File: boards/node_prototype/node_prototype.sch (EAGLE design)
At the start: 28 parts, among them T1 2N2222, X1 BU-SMA-H

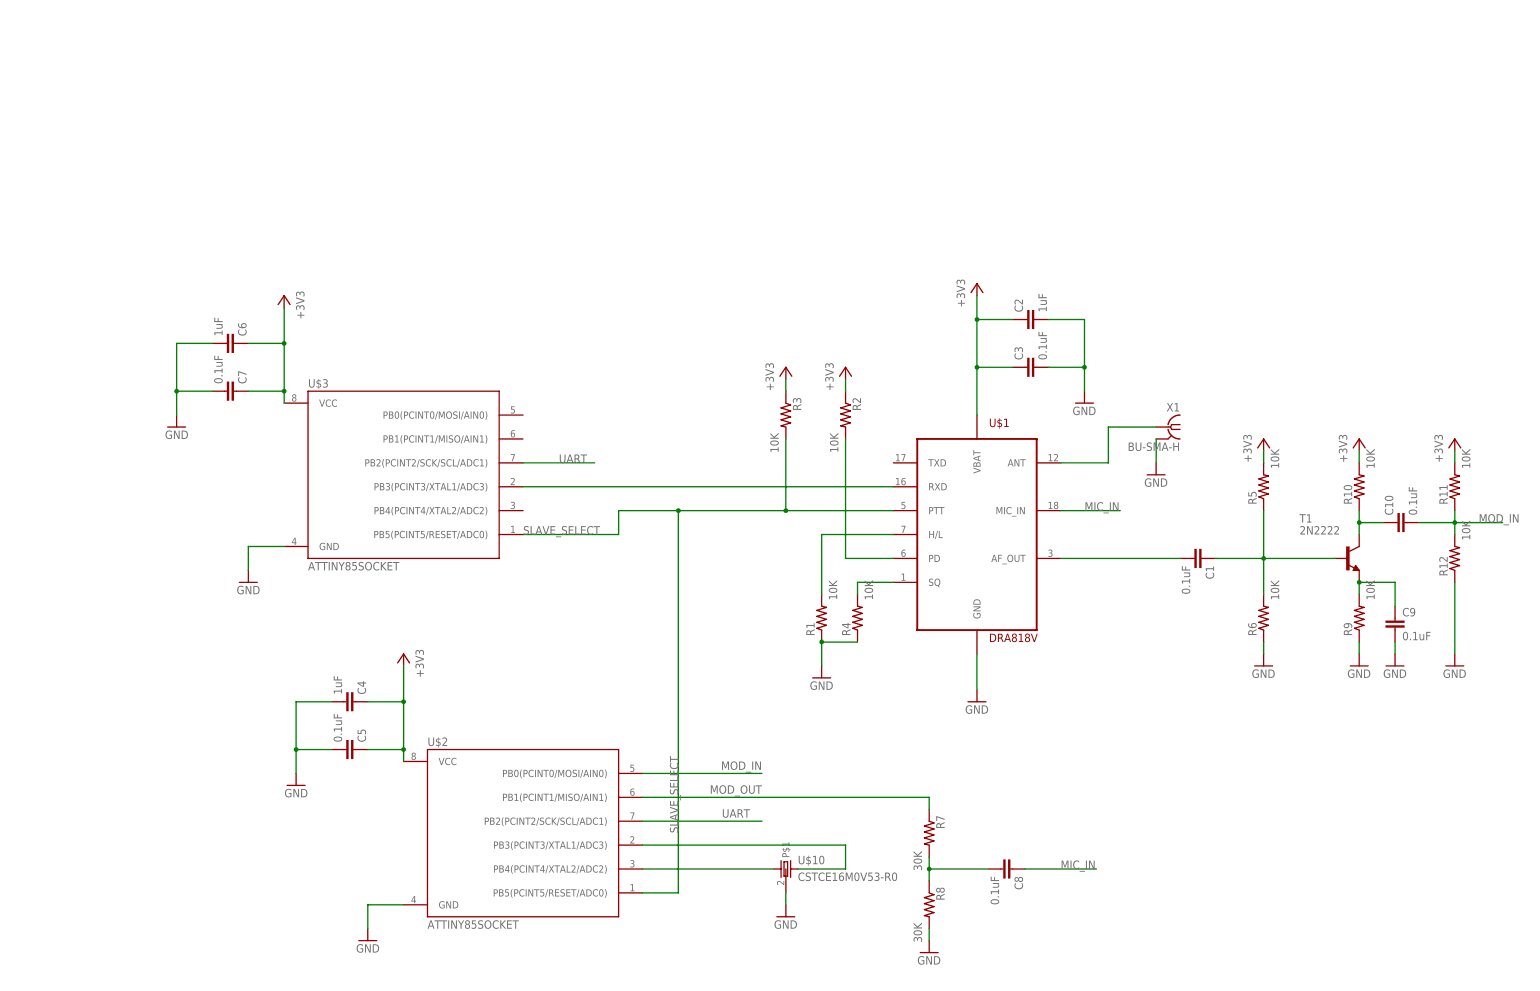
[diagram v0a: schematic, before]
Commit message: rename rocket radio, add renders
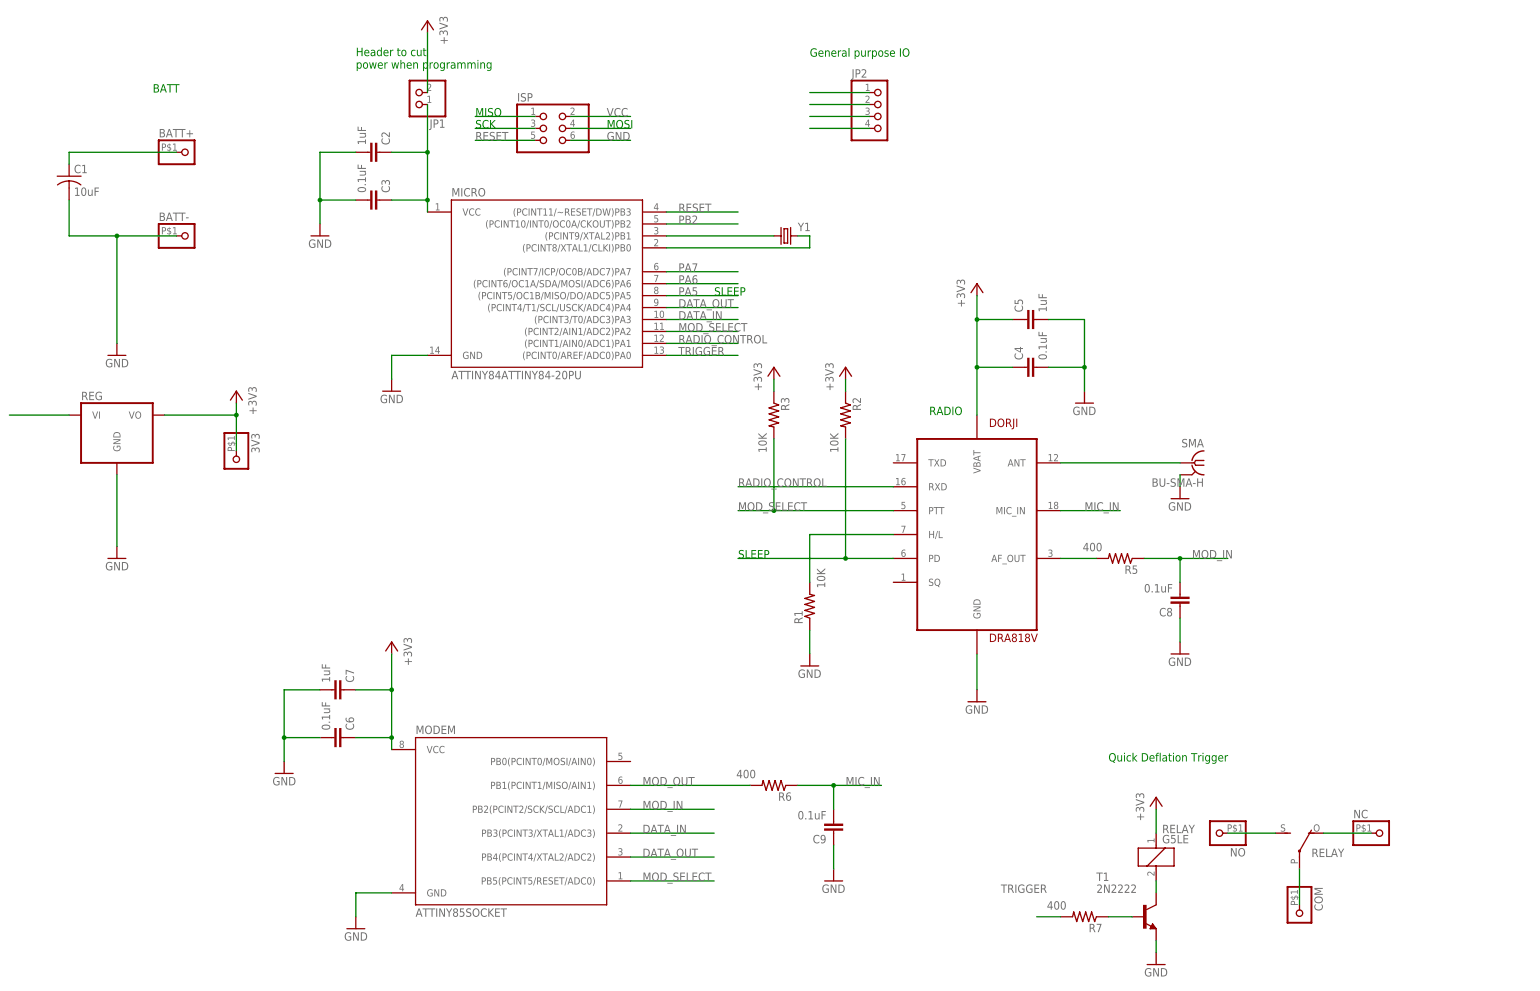
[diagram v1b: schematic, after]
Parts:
- removed C10: 0.1uF, rcl:C-EUC0603
- removed R10, R11, R12, R4, R9: 10K, rcl:R-US_R0603
- removed R8: 30K, rcl:R-US_R0603
- removed U$10: CSTCE16M0V53-R0, evan:CSTCE16M0V53-R0
- removed U$2, U$3: ATTINY85SOCKET, evan:ATTINY85SOCKET
- removed X1: BU-SMA-H, con-coax:BU-SMA-H
- added 3V3, BATT+, BATT-, COM, NC, NO: (no value), evan:PINHD-1X1
- added ISP: (no value), pinhead:PINHD-2X3
- added JP1: (no value), pinhead:PINHD-1X2
- added JP2: (no value), pinhead:PINHD-1X4
- added MICRO: ATTINY84ATTINY84-20PU, evan:ATTINY84ATTINY84-20PU
- added MODEM: ATTINY85SOCKET, evan:ATTINY85SOCKET
- added REG: AP1117-3.3SOT223, evan:AP1117-3.3SOT223
- added RELAY: G5LE, relay:G5LE
- added SMA: BU-SMA-H, con-coax:BU-SMA-H
- added Y1: (no value), evan:CRYSTAL
- C1: value 0.1uF -> 10uF; device rcl:C-EUC0603 -> rcl:C-US025-050X050
- C4, C6: value 1uF -> 0.1uF
- C5, C7: value 0.1uF -> 1uF
- R5, R6: value 10K -> 400
- R7: value 30K -> 400
- renumbered U$1 to DORJI
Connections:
- removed net N$17: U$10.2, U$2.PB3(PCINT3/XTAL1/ADC3)
- removed net N$18: U$10.1, U$2.PB4(PCINT4/XTAL2/ADC2)
- removed net N$3: DORJI.PD, R2.2
- removed net N$5: DORJI.SQ, R4.2
- removed net SLAVE_SELECT: DORJI.PTT, R3.2, U$2.PB5(PCINT5/RESET/ADC0), U$3.PB5(PCINT5/RESET/ADC0)
- removed net UART: U$2.PB2(PCINT2/SCK/SCL/ADC1), U$3.PB2(PCINT2/SCK/SCL/ADC1)
- new net BATT: BATT+.1, C1.1, REG.VI
- new net DATA_IN: MICRO.(PCINT3/T0/ADC3)PA3, MODEM.PB3(PCINT3/XTAL1/ADC3)
- new net DATA_OUT: ISP.3, MICRO.(PCINT4/T1/SCL/USCK/ADC4)PA4, MODEM.PB4(PCINT4/XTAL2/ADC2)
- new net MOD_SELECT: DORJI.PTT, MICRO.(PCINT2/AIN1/ADC2)PA2, MODEM.PB5(PCINT5/RESET/ADC0), R3.2
- new net N$12: MICRO.(PCINT8/XTAL1/CLKI)PB0, Y1.2
- new net N$4: DORJI.AF_OUT, R5.2
- new net PA5: DORJI.PD, ISP.1, JP2.4, MICRO.(PCINT5/OC1B/MISO/DO/ADC5)PA5, R2.2
- new net PA6: ISP.4, JP2.3, MICRO.(PCINT6/OC1A/SDA/MOSI/ADC6)PA6
- new net PA7: JP2.2, MICRO.(PCINT7/ICP/OC0B/ADC7)PA7
- new net PB2: JP2.1, MICRO.(PCINT10/INT0/OC0A/CKOUT)PB2
- new net RADIO_CONTROL: DORJI.RXD, MICRO.(PCINT1/AIN0/ADC1)PA1
- new net RESET: ISP.5, MICRO.(PCINT11/~RESET/DW)PB3
- new net TRIGGER: MICRO.(PCINT0/AREF/ADC0)PA0, R7.2
- new net VCC: C2.1, C3.1, ISP.2, JP1.1, MICRO.VCC
- net +3V3: now also 3V3.1, JP1.2, MODEM.VCC, REG.VO, RELAY1.1; no longer C2.1, C3.1, R10.2, R11.2, R5.2, U$2.VCC, U$3.VCC
- net GND: now also BATT-.1, C1.2, C8.1, C9.1, ISP.6, MICRO.GND, MODEM.GND, REG.GND, SMA.2, T1.E; no longer C9.2, R12.1, R4.1, R6.1, R8.2, R9.1, U$10.P$1, U$2.GND, U$3.GND, X1.2
- net MIC_IN: now also C9.2, R6.1; no longer C8.1
- net MOD_IN: now also C8.2, MODEM.PB2(PCINT2/SCK/SCL/ADC1), R5.1; no longer C10.2, R11.1, R12.2, U$2.PB0(PCINT0/MOSI/AIN0)
- net MOD_OUT: now also MODEM.PB1(PCINT1/MISO/AIN1), R6.2; no longer R7.1, U$2.PB1(PCINT1/MISO/AIN1)
- net N$1: now also SMA.1; no longer X1.1
- net N$10: now also NC.1, RELAY2.O; no longer C9.1, R9.2, T1.E
- net N$11: now also COM.1, RELAY2.P; no longer C10.1, R10.1, T1.C
- net N$6: now also R7.1, T1.B; no longer C8.2, R7.2, R8.1
- net N$7: now also RELAY1.2, T1.C; no longer C1.1, R5.1, R6.2, T1.B
- net N$8: now also MICRO.(PCINT9/XTAL2)PB1, Y1.1; no longer C1.2, DORJI.AF_OUT
- net N$9: now also NO.1, RELAY2.S; no longer DORJI.RXD, U$3.PB3(PCINT3/XTAL1/ADC3)
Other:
- note added: "BATT"
- note added: "General purpose IO"
- note added: "Header to cut power when programming"
- note added: "MISO"
- note added: "MOSI"
- note added: "Quick Deflation Trigger"
- note added: "RADIO"
- note added: "SCK"
- note added: "SLEEP"
- moved on the sheet: C1, C2, C3, C4, C5, C6, C7, C8, C9, R1, R3, R5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
